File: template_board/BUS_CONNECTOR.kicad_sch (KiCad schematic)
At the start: 1 part, among them J2 PTHF-130-02-G-Q-368

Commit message: chamt skończony chyba
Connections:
- net GND: now also J2.1, J2.13, J2.14, J2.15, J2.16, J2.2, J2.25, J2.26, J2.27, J2.28, J2.3, J2.37, J2.38, J2.39, J2.4, J2.40, J2.49, J2.50, J2.51, J2.52, J2.77, J2.78, J2.79, J2.80; no longer J2.30
- net +VREZ: now reaches J2.10
- net +VREZ: now also J2.11, J2.12, J2.5, J2.6, J2.7, J2.8, J2.9
- net GPIO19: now reaches J2.100
- net GPIO20: now reaches J2.101
- net GPIO21: now reaches J2.102
- net GPIO22: now reaches J2.103
- net GPIO23: now reaches J2.104
- net GPIO24: now reaches J2.105
- net GPIO25: now reaches J2.106
- net GPIO26: now reaches J2.107
- net GPIO27: now reaches J2.108
- net GPIO28: now reaches J2.109
- net GPIO29: now reaches J2.110
- net GPIO30: now reaches J2.111
- net GPIO31: now reaches J2.112
- net GPIO32: now reaches J2.113
- net GPIO33: now reaches J2.114
- net GPIO34: now reaches J2.115
- net GPIO35: now reaches J2.116
- net +VCC: now reaches J2.17
- net +VCC: now also J2.18, J2.19, J2.20, J2.21, J2.22, J2.23, J2.24
- net +5V_unprotected: now reaches J2.29
- net +5V_unprotected: now also J2.30, J2.31, J2.32, J2.33, J2.34, J2.35, J2.36
- net CAN1.+: now reaches J2.41
- net CAN2.+: now reaches J2.42
- net CAN3.+: now reaches J2.43
- net CAN4.+: now reaches J2.44
- net CAN1.-: now reaches J2.45
- net CAN2.-: now reaches J2.46
- net CAN3.-: now reaches J2.47
- net CAN4.-: now reaches J2.48
- net USB1.D+: now reaches J2.53
- net USB2.D+: now reaches J2.54
- net USB3.D+: now reaches J2.55
- net USB4.D+: now reaches J2.56
- net USB1.D-: now reaches J2.57
- net USB2.D-: now reaches J2.58
- net USB3.D-: now reaches J2.59
- net USB4.D-: now reaches J2.60
- net USB5.D+: now reaches J2.61
- net USB6.D+: now reaches J2.62
- net USB7.D+: now reaches J2.63
- net USB8.D+: now reaches J2.64
- net USB5.D-: now reaches J2.65
- net USB6.D-: now reaches J2.66
- net USB7.D-: now reaches J2.67
- net USB8.D-: now reaches J2.68
- net USB9.D+: now reaches J2.69
- net USB10.D+: now reaches J2.70
- net USB11.D+: now reaches J2.71
- net USB12.D+: now reaches J2.72
- net USB9.D-: now reaches J2.73
- net USB10.D-: now reaches J2.74
- net USB11.D-: now reaches J2.75
- net USB12.D-: now reaches J2.76
- net GPIO0: now reaches J2.81
- net GPIO1: now reaches J2.82
- net GPIO2: now reaches J2.83
- net GPIO3: now reaches J2.84
- net GPIO4: now reaches J2.85
- net GPIO5: now reaches J2.86
- net GPIO6: now reaches J2.87
- net GPIO7: now reaches J2.88
- net GPIO8: now reaches J2.89
- net GPIO9: now reaches J2.90
- net GPIO10: now reaches J2.91
- net GPIO11: now reaches J2.92
- net GPIO12: now reaches J2.93
- net GPIO13: now reaches J2.94
- net GPIO14: now reaches J2.95
- net GPIO15: now reaches J2.96
- net GPIO16: now reaches J2.97
- net GPIO17: now reaches J2.98
- net GPIO18: now reaches J2.99
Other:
- note added: "+ - CAN[1-4]"
- note added: "+ - USB[1-12]"
- note added: "5V"
- note added: "GND"
- note added: "GPIO [0-35]"
- note added: "VCC"
- note added: "VREZ"
- moved on the sheet: J2

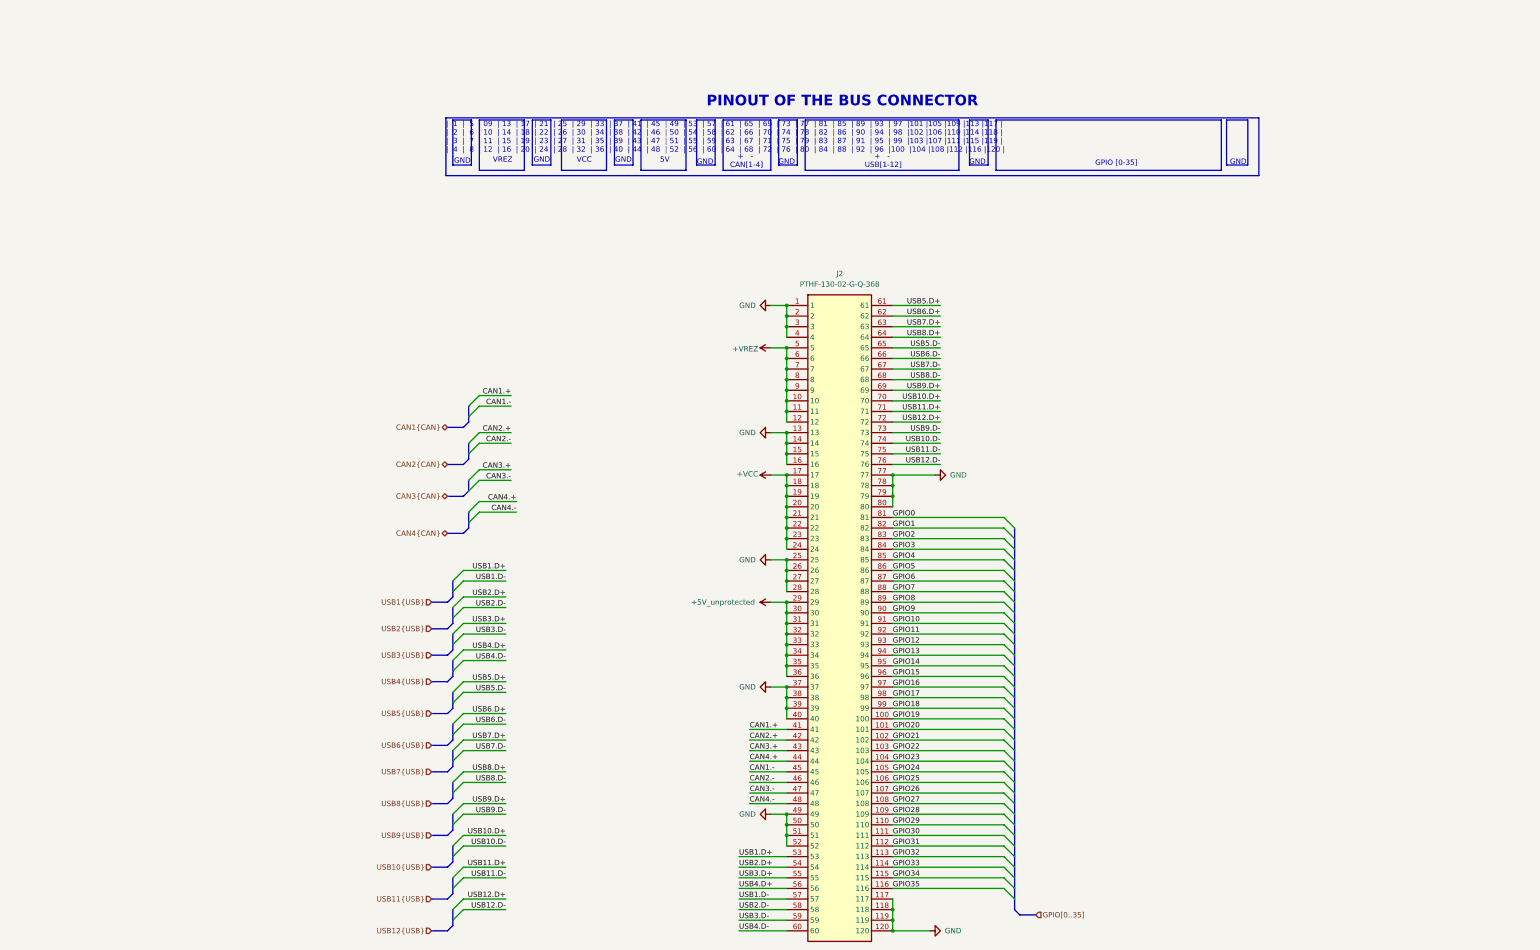
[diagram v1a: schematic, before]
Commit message: sub leyoyut partially completed
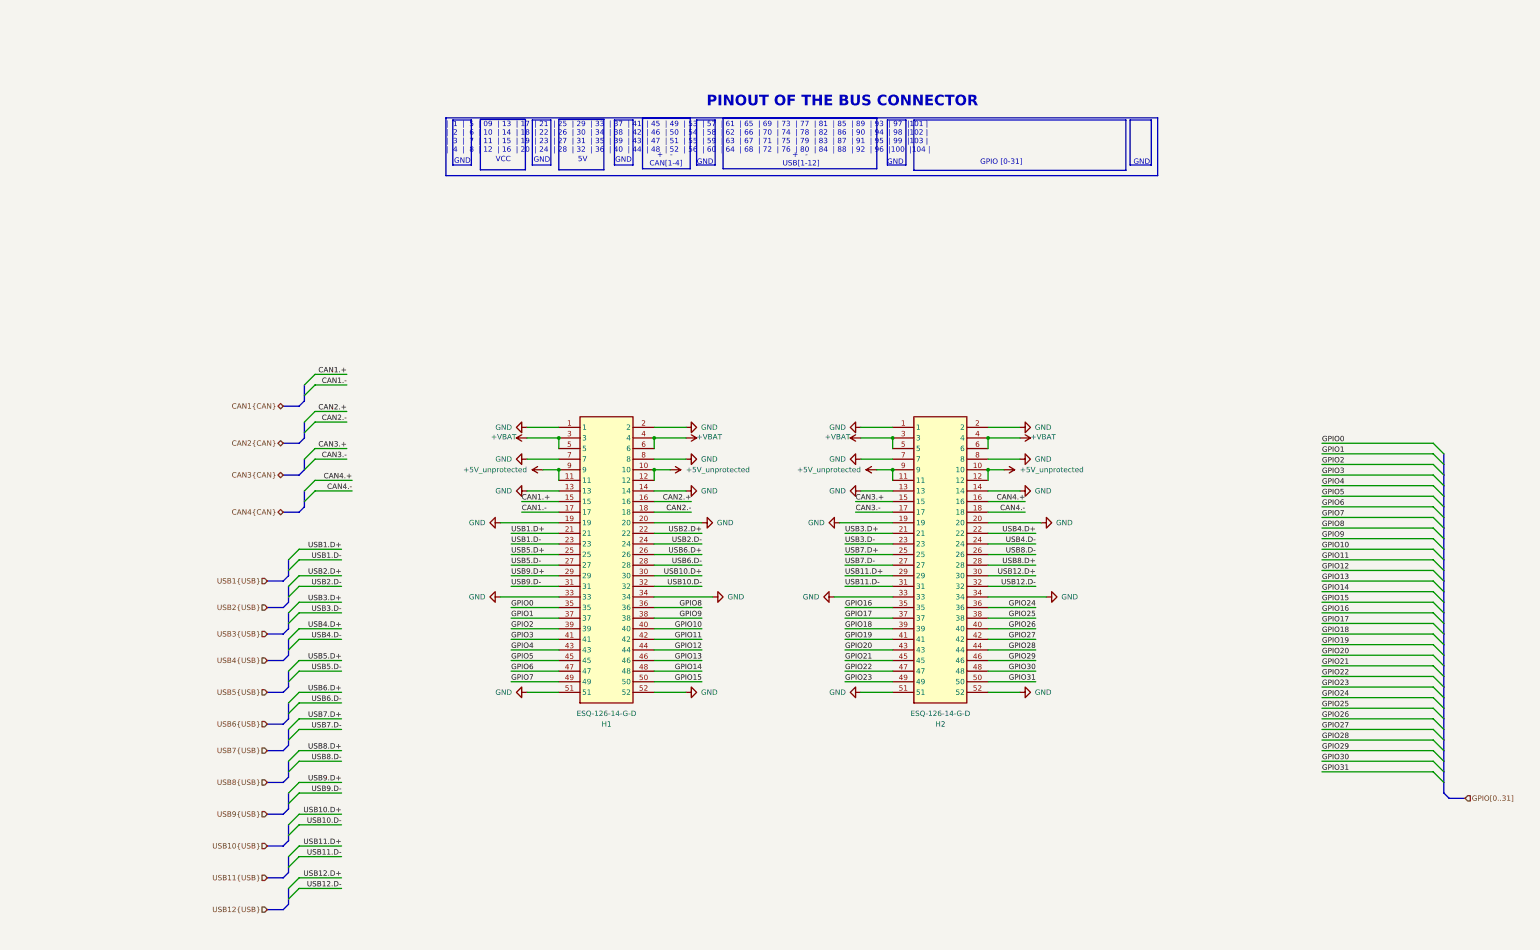
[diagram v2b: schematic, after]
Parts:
- removed J2: PTHF-130-02-G-Q-368, lib:PTHF13002GQ368, symbol PTHF-130-02-G-Q-368:PTHF-130-02-G-Q-368
- added H1, H2: ESQ-126-14-G-D, lib:ESQ-126-Y-X-D, symbol ESQ-126-14-G-D:ESQ-126-14-G-D
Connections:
- net +5V_unprotected: now also H1.10, H1.11, H1.12, H1.9, H2.10, H2.11, H2.12, H2.9
- net CAN1.+: now also H1.15
- net CAN1.-: now also H1.17
- net CAN2.+: now also H1.16
- net CAN2.-: now also H1.18
- net CAN3.+: now also H2.15
- net CAN3.-: now also H2.17
- net CAN4.+: now also H2.16
- net CAN4.-: now also H2.18
- net GND: now also H1.1, H1.13, H1.14, H1.19, H1.2, H1.20, H1.33, H1.34, H1.51, H1.52, H1.7, H1.8, H2.1, H2.13, H2.14, H2.19, H2.2, H2.20, H2.33, H2.34, H2.51, H2.52, H2.7, H2.8
- net GPIO0: now also H1.35
- net GPIO1: now also H1.37
- net GPIO10: now also H1.40
- net GPIO11: now also H1.42
- net GPIO12: now also H1.44
- net GPIO13: now also H1.46
- net GPIO14: now also H1.48
- net GPIO15: now also H1.50
- net GPIO16: now also H2.35
- net GPIO17: now also H2.37
- net GPIO18: now also H2.39
- net GPIO19: now also H2.41
- net GPIO2: now also H1.39
- net GPIO20: now also H2.43
- net GPIO21: now also H2.45
- net GPIO22: now also H2.47
- net GPIO23: now also H2.49
- net GPIO24: now also H2.36
- net GPIO25: now also H2.38
- net GPIO26: now also H2.40
- net GPIO27: now also H2.42
- net GPIO28: now also H2.44
- net GPIO29: now also H2.46
- net GPIO3: now also H1.41
- net GPIO30: now also H2.48
- net GPIO31: now also H2.50
- net GPIO4: now also H1.43
- net GPIO5: now also H1.45
- net GPIO6: now also H1.47
- net GPIO7: now also H1.49
- net GPIO8: now also H1.36
- net GPIO9: now also H1.38
- net USB1.D+: now also H1.21
- net USB1.D-: now also H1.23
- net USB10.D+: now also H1.30
- net USB10.D-: now also H1.32
- net USB11.D+: now also H2.29
- net USB11.D-: now also H2.31
- net USB12.D+: now also H2.30
- net USB12.D-: now also H2.32
- net USB2.D+: now also H1.22
- net USB2.D-: now also H1.24
- net USB3.D+: now also H2.21
- net USB3.D-: now also H2.23
- net USB4.D+: now also H2.22
- net USB4.D-: now also H2.24
- net USB5.D+: now also H1.25
- net USB5.D-: now also H1.27
- net USB6.D+: now also H1.26
- net USB6.D-: now also H1.28
- net USB7.D+: now also H2.25
- net USB7.D-: now also H2.27
- net USB8.D+: now also H2.28
- net USB8.D-: now also H2.26
- net USB9.D+: now also H1.29
- net USB9.D-: now also H1.31
- new net +VBAT: H1.3, H1.4, H1.5, H1.6, H2.3, H2.4, H2.5, H2.6
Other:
- note added: "GPIO [0-31]"
- note added: "| 1 | 5 | 09 | 13 | 17 | 21 | 25 | 29 | 33 | 37 | 41 | 45 | 49 | 53 | 57 | 61 | 65 | 69 | 73 | 77 | 81 | 85 | 89 | 93 | 97 |101 | | 2 | 6 | 10 | 14 | 18 | 22 | 26 | 30 | 34 | 38 | 42 | 46 | 50 | 54 | 58 | 62 | 66 | 70 | 74 | 78 | 82 | 86 | 90 | 94 | 98 |102 | | 3 | 7 | 11 | 15 | 19 | 23 | 27 | 31 | 35 | 39 | 43 | 47 | 51 | 55 | 59 | 63 | 67 | 71 | 75 | 79 | 83 | 87 | 91 | 95 | 99 |103 | | 4 | 8 |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"
- note removed: "GPIO [0-35]"
- note removed: "VREZ"
- note removed: "| 1 | 5 | 09 | 13 | 17 | 21 | 25 | 29 | 33 | 37 | 41 | 45 | 49 | 53 | 57 | 61 | 65 | 69 | 73 | 77 | 81 | 85 | 89 | 93 | 97 |101 |105 |109 |113 |117 | | 2 | 6 | 10 | 14 | 18 | 22 | 26 | 30 | 34 | 38 | 42 | 46 | 50 | 54 | 58 | 62 | 66 | 70 | 74 | 78 | 82 | 86 | 90 | 94 | 98 |102 |106 |110 |114 |118 | | 3 | 7 | 11 | 15 | 19 | 23 | 27 | 31 | 35 | 39 | 43 | 47 | 51 | 55 | 59 | 63 | 67 | 71 | 75 | 79 |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"
